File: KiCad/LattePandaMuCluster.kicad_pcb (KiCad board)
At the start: 2 copper layers, 203.2 x 170.2 mm, 721 parts, among them J1 ATX-24, J10 Bus_M.2_Socket_M, J11 Bus_M.2_Socket_M, J12 Bus_M.2_Socket_M, J13 Bus_M.2_Socket_M, J14 Bus_M.2_Socket_M, J15 Conn_02x05_Odd_Even, J17 Conn_01x04, J18 Conn_01x04, J19 RJ45_LED_Shielded_x2, J2 Conn_02x04_Top_Bottom, J20 RJE361882415, J21 RJ45_LED_Shielded_x2, J22 USB3_A_Stacked, J23 USB3_IDC, J24 Conn_02x05_Odd_Even, J26 HDMI_A, J27 JACK-USBE-20PINTL, J3 SFF-8087, J4 SFF-8087, J5 SATA, J6 Bus_M.2_Socket_E, J7 Bus_M.2_Socket_E, J8 Bus_PCI_Express_x4, J9 Bus_PCI_Express_x4, M1 Fan_4pin, M10 Fan_4pin, M2 Fan_4pin, M3 Fan_4pin, M4 Fan_4pin, M5 Fan_4pin, M6 Fan_4pin, M7 Fan_4pin, M8 Fan_4pin, M9 Fan_4pin, Q1 2N7002, Q2 2N7002, Q3 2N7002, U1 ZD25Q64BSIGT, U10 H5VU25U, U11 H5VU25U, U12 KTI226V, U13 KTI226V, U14 ZD25Q64BSIGT, U15 ZD25Q64BSIGT, U16 H5VU25U, U17 H5VU25U, U18 H5VU25U, U19 H5VU25U, U2 ZD25Q64BSIGT, U20 KTI226V, U21 KTI226V, U22 ZD25Q64BSIGT, U23 ZD25Q64BSIGT, U24 H5VU25U, U25 H5VU25U, U26 KTI226V, U27 ZD25Q64BSIGT, U28 H5VU25U, U29 H5VU25U, U3 ZD25Q64BSIGT, U30 H5VU25U, U31 H5VU25U, U32 H5VU25U, U33 H5VU25U, U34 H5VU25U, U35 H5VU25U, U36 H5VU25U, U37 H5VU25U, U38 H5VU25U, U39 H5VU25U, U4 ZD25Q64BSIGT, U40 TPS65987DDJRSHR, U41 H5VU25U, U42 H5VU25U, U43 ZD25Q64BSIGT, U44 H5VU25U, U5 ZD25Q64BSIGT, U6 TPS54331, U7 STM32F030C8Tx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

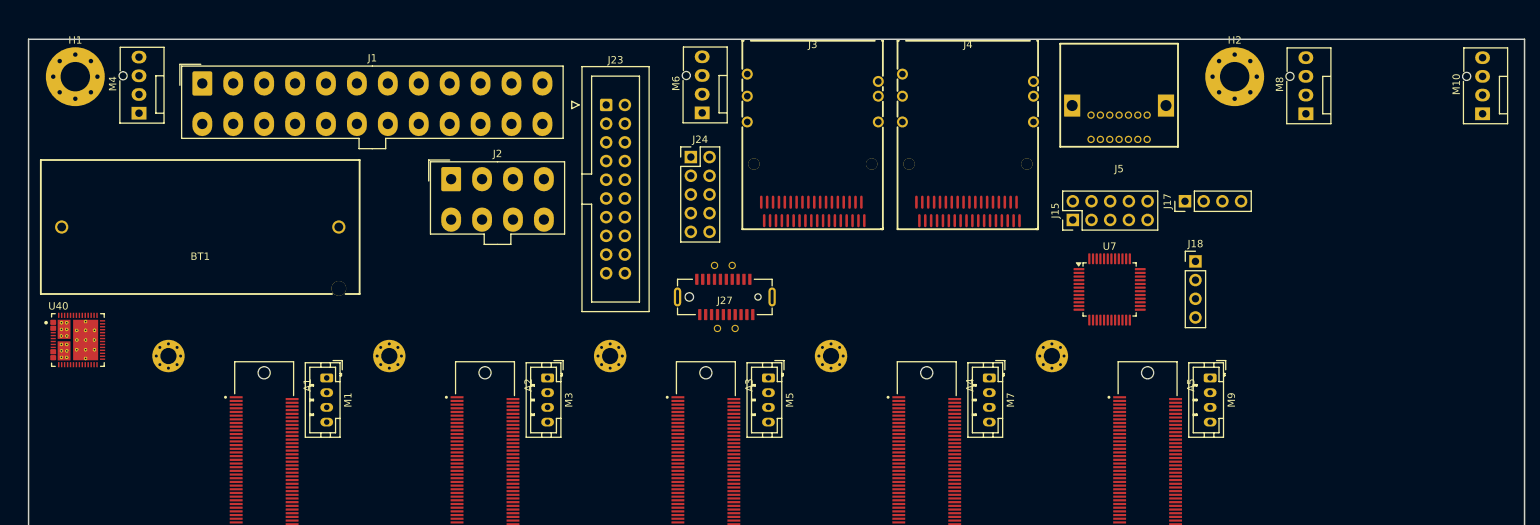
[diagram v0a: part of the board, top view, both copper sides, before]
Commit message: Lay out Headers
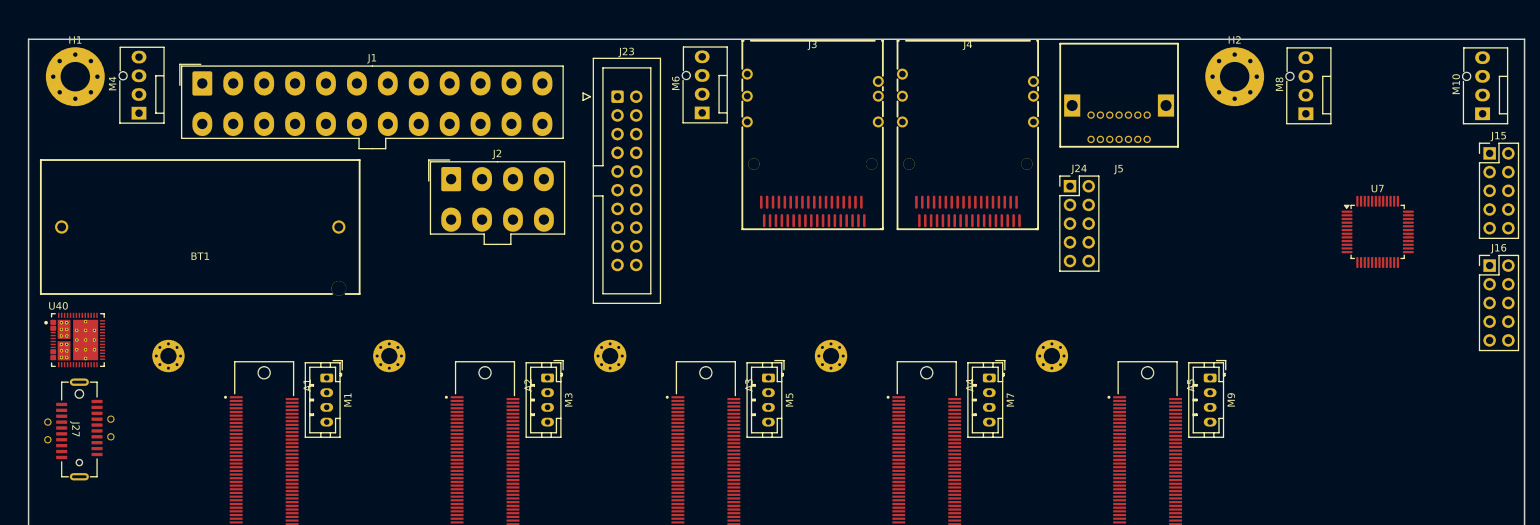
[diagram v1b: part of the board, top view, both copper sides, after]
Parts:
- removed J17, J18: Conn_01x04, Connector_PinHeader_2.54mm:PinHeader_1x04_P2.54mm_Vertical
- added J16: Conn_02x05_Odd_Even, Connector_PinHeader_2.54mm:PinHeader_2x05_P2.54mm_Vertical, F.Cu at (298.5, 80.7)
- moved J27 89.5 mm to (106.9, 103.0), turned to 90 degrees
- moved J15 57.3 mm to (298.5, 65.5), turned to 0 degrees
- moved J24 51.7 mm to (241.5, 70.0)
- moved U7 37.2 mm to (283.2, 76.2)
- moved J23 1.90 mm to (180.0, 57.8)
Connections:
- net /Module 1/TYPE_C_HEADER.SBU1 renamed /Module 1/TYPE_C_HEADER.SBU2
- J15 pad 9: unconnected-(J15-Pin_9-Pad9) -> +5VSB

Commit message: Start placing capacitors
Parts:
- moved C4 217.7 mm to (126.0, 102.5)
- moved C3 217.6 mm to (126.0, 101.5)
- moved D27 206.3 mm to (283.5, 67.0)
- moved L1 171.5 mm to (155.5, 79.5), turned to 180 degrees
- moved U6 166.7 mm to (154.0, 70.0), turned to -90 degrees
- moved U43 88.2 mm to (114.0, 106.5), turned to -90 degrees
- moved J1 47.9 mm to (171.2, 61.5), turned to 180 degrees
- moved U40 16.1 mm to (105.4, 106.9)
- moved J2 15.9 mm to (165.0, 83.0), turned to 90 degrees
- moved J27 10.3 mm to (105.5, 92.8)
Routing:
- net Net-(A1-HSIO0_TX-): track 0.00 -> 1.88 mm
- net Net-(A1-HSIO0_TX+): track 0.00 -> 1.75 mm
- added copper zone on In1.Cu, net GND
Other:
- copper layers 2 -> 4

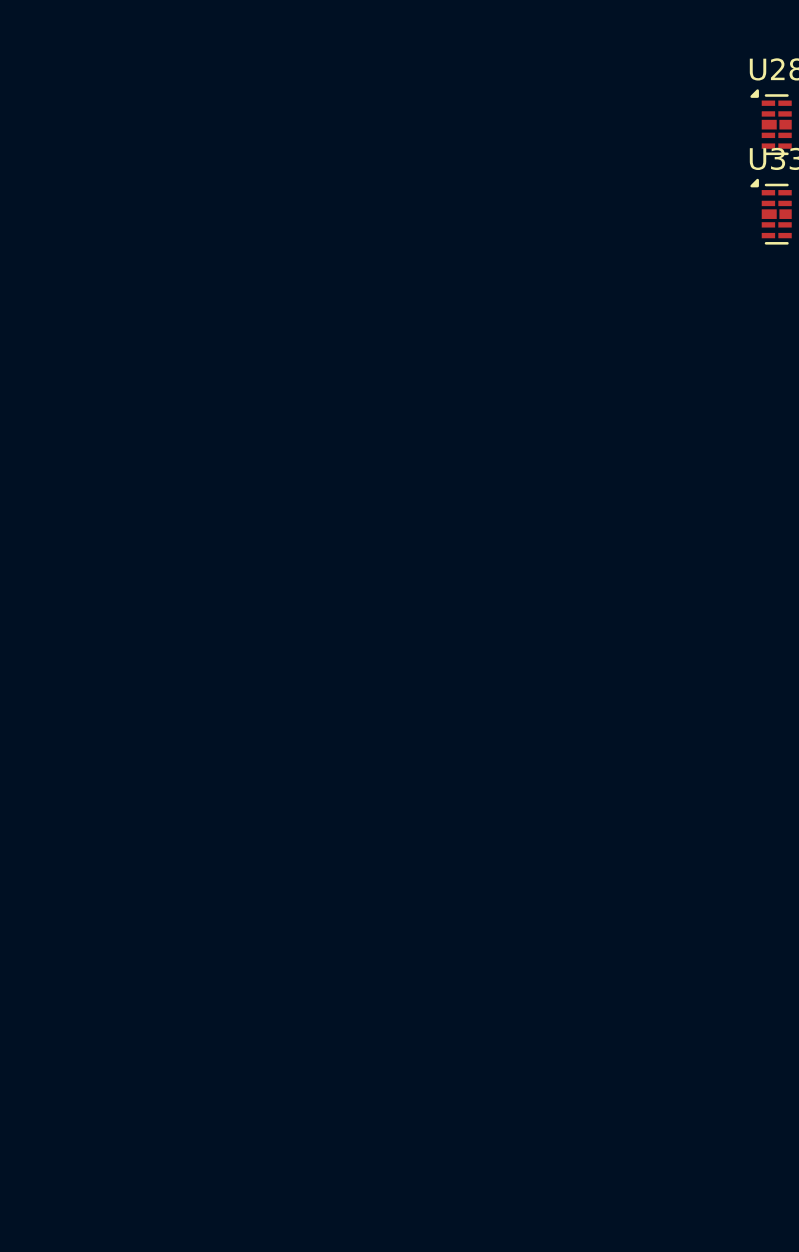
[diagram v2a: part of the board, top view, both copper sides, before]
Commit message: Finish connecting x1 slot. Add pcie clkreq lines
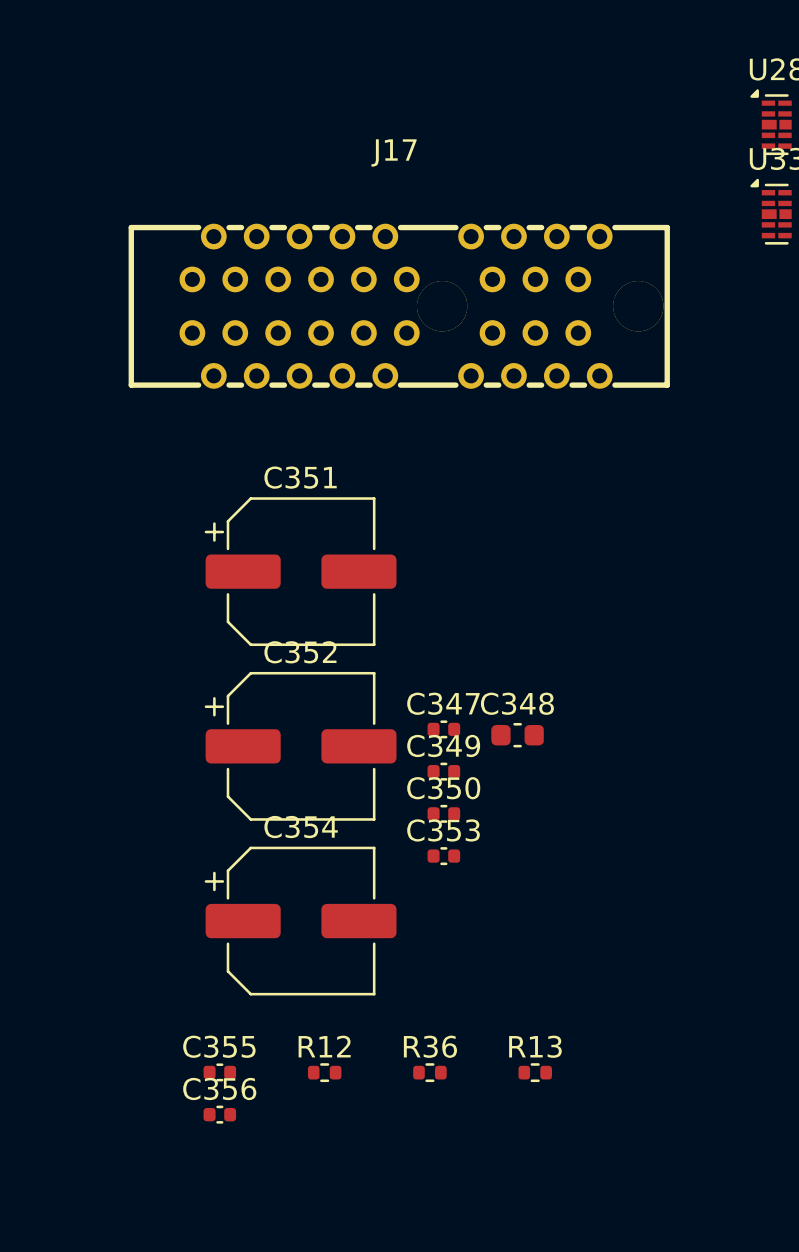
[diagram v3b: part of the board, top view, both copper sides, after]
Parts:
- added C347: 100nF/50V, Capacitor_SMD:C_0402_1005Metric, F.Cu at (60.2, 124.0)
- added C348: 10uF/10V, Capacitor_SMD:C_0603_1608Metric, F.Cu at (63.7, 124.3)
- added C349: 100nF/50V, Capacitor_SMD:C_0402_1005Metric, F.Cu at (60.2, 126.0)
- added C350: 100nF/50V, Capacitor_SMD:C_0402_1005Metric, F.Cu at (60.2, 127.9)
- added C351: 100uF/25V, Capacitor_SMD:CP_Elec_6.3x7.7, F.Cu at (53.6, 116.6)
- added C352: 100uF/25V, Capacitor_SMD:CP_Elec_6.3x7.7, F.Cu at (53.6, 124.8)
- added C353: 100nF/50V, Capacitor_SMD:C_0402_1005Metric, F.Cu at (60.2, 129.9)
- added C354: 560uF/25V, Capacitor_SMD:CP_Elec_6.3x7.7, F.Cu at (53.6, 132.9)
- added C355: 220nF, Capacitor_SMD:C_0402_1005Metric, F.Cu at (49.8, 140.0)
- added C356: 220nF, Capacitor_SMD:C_0402_1005Metric, F.Cu at (49.8, 142.0)
- added J17: Bus_PCI_Express_x1, EasyEDA2KiCAD:CONN-TH_HYCW05-PCI36-155B, F.Cu at (58.0, 104.2)
- added R12: 10k, Resistor_SMD:R_0402_1005Metric, F.Cu at (54.7, 140.0)
- added R13: 10k, Resistor_SMD:R_0402_1005Metric, F.Cu at (64.5, 140.0)
- added R36: 10k, Resistor_SMD:R_0402_1005Metric, F.Cu at (59.6, 140.0)
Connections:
- net /Module 1/TYPE_C_HEADER.SBU2 renamed /Module 1/TYPE_C_HEADER.SBU1
- net /Module 4/ETH.SMBCLK renamed /Module 4/PCIE_X4.SMBCLK
- net /Module 4/ETH.SMBDAT renamed /Module 4/PCIE_X4.SMBDAT
- A1 pad 100: Net-(A1-~{CLKREQ3}) -> /Module 1/ETH.~{CLKREQ}
- A1 pad 102: Net-(A1-~{CLKREQ4}) -> /Module 1/M2_EKEY.~{CLKREQ}
- A1 pad 25: unconnected-(A1-HSIO2_TX+-Pad25) -> Net-(A1-HSIO2_TX+)
- A1 pad 27: unconnected-(A1-HSIO2_TX--Pad27) -> Net-(A1-HSIO2_TX-)
- A1 pad 28: unconnected-(A1-HSIO2_RX+-Pad28) -> /Module 1/M2_EKEY.Rx0+
- A1 pad 30: unconnected-(A1-HSIO2_RX--Pad30) -> /Module 1/M2_EKEY.Rx0-
- A1 pad 85: /Module 1/ETH.REFCLK+ -> unconnected-(A1-REFCLK0+-Pad85)
- A1 pad 87: /Module 1/ETH.REFCLK- -> unconnected-(A1-REFCLK0--Pad87)
- A1 pad 88: unconnected-(A1-REFCLK3+-Pad88) -> /Module 1/ETH.REFCLK+
- A1 pad 90: unconnected-(A1-REFCLK3--Pad90) -> /Module 1/ETH.REFCLK-
- A1 pad 91: /Module 1/NVME.REFCLK+ -> unconnected-(A1-REFCLK1+-Pad91)
- A1 pad 93: /Module 1/NVME.REFCLK- -> unconnected-(A1-REFCLK1--Pad93)
- A1 pad 94: unconnected-(A1-REFCLK4+-Pad94) -> /Module 1/M2_EKEY.REFCLK+
- A1 pad 96: unconnected-(A1-REFCLK4--Pad96) -> /Module 1/M2_EKEY.REFCLK-
- A1 pad 97: unconnected-(A1-REFCLK2+-Pad97) -> /Module 1/NVME.REFCLK+
- A1 pad 99: unconnected-(A1-REFCLK2--Pad99) -> /Module 1/NVME.REFCLK-
- A2 pad 100: Net-(A2-~{CLKREQ3}) -> /Module 2/ETH.~{CLKREQ}
- A2 pad 102: Net-(A2-~{CLKREQ4}) -> /Module 2/M2_EKEY.~{CLKREQ}
- A2 pad 85: /Module 2/ETH.REFCLK+ -> unconnected-(A2-REFCLK0+-Pad85)
- A2 pad 87: /Module 2/ETH.REFCLK- -> unconnected-(A2-REFCLK0--Pad87)
- A2 pad 88: unconnected-(A2-REFCLK3+-Pad88) -> /Module 2/ETH.REFCLK+
- A2 pad 90: unconnected-(A2-REFCLK3--Pad90) -> /Module 2/ETH.REFCLK-
- A2 pad 91: /Module 2/NVME.REFCLK+ -> unconnected-(A2-REFCLK1+-Pad91)
- A2 pad 93: /Module 2/NVME.REFCLK- -> unconnected-(A2-REFCLK1--Pad93)
- A2 pad 94: unconnected-(A2-REFCLK4+-Pad94) -> /Module 2/M2_EKEY.REFCLK+
- A2 pad 96: unconnected-(A2-REFCLK4--Pad96) -> /Module 2/M2_EKEY.REFCLK-
- A2 pad 97: /Module 2/M2_EKEY.REFCLK+ -> /Module 2/NVME.REFCLK+
- A2 pad 99: /Module 2/M2_EKEY.REFCLK- -> /Module 2/NVME.REFCLK-
- A3 pad 100: Net-(A3-~{CLKREQ3}) -> /Module 3/ETH.~{CLKREQ}
- A3 pad 28: /Module 3/M2_EKEY.Rx0+ -> /Module 3/PCIE_X1.Rx0+
- A3 pad 30: /Module 3/M2_EKEY.Rx0- -> /Module 3/PCIE_X1.Rx0-
- A3 pad 79: /Module 3/M2_EKEY.USB-D- -> /Module 3/PCIE_X1.USB-D-
- A3 pad 81: /Module 3/M2_EKEY.USB-D+ -> /Module 3/PCIE_X1.USB-D+
- A3 pad 85: /Module 3/ETH.REFCLK+ -> unconnected-(A3-REFCLK0+-Pad85)
- A3 pad 87: /Module 3/ETH.REFCLK- -> unconnected-(A3-REFCLK0--Pad87)
- A3 pad 88: unconnected-(A3-REFCLK3+-Pad88) -> /Module 3/ETH.REFCLK+
- A3 pad 90: unconnected-(A3-REFCLK3--Pad90) -> /Module 3/ETH.REFCLK-
- A3 pad 91: /Module 3/NVME.REFCLK+ -> unconnected-(A3-REFCLK1+-Pad91)
- A3 pad 93: /Module 3/NVME.REFCLK- -> unconnected-(A3-REFCLK1--Pad93)
- A3 pad 94: unconnected-(A3-REFCLK4+-Pad94) -> /Module 3/PCIE_X1.REFCLK+
- A3 pad 96: unconnected-(A3-REFCLK4--Pad96) -> /Module 3/PCIE_X1.REFCLK-
- A3 pad 97: /Module 3/M2_EKEY.REFCLK+ -> /Module 3/NVME.REFCLK+
- A3 pad 99: /Module 3/M2_EKEY.REFCLK- -> /Module 3/NVME.REFCLK-
- A4 pad 100: Net-(A4-~{CLKREQ3}) -> /Module 4/ETH.~{CLKREQ}
- A4 pad 22: /Module 4/PCIE_X4.Rx1+ -> /Module 4/PCIE_X4.RX4+
- A4 pad 24: /Module 4/PCIE_X4.Rx1- -> /Module 4/PCIE_X4.RX4-
- A4 pad 46: /Module 4/NVME.Rx1+ -> /Module 4/NVME.RX4+
- A4 pad 48: /Module 4/NVME.Rx1- -> /Module 4/NVME.RX4-
- A4 pad 85: /Module 4/ETH.REFCLK+ -> unconnected-(A4-REFCLK0+-Pad85)
- A4 pad 87: /Module 4/ETH.REFCLK- -> unconnected-(A4-REFCLK0--Pad87)
- A4 pad 88: unconnected-(A4-REFCLK3+-Pad88) -> /Module 4/ETH.REFCLK+
- A4 pad 90: unconnected-(A4-REFCLK3--Pad90) -> /Module 4/ETH.REFCLK-
- A4 pad 91: /Module 4/NVME.REFCLK+ -> unconnected-(A4-REFCLK1+-Pad91)
- A4 pad 93: /Module 4/NVME.REFCLK- -> unconnected-(A4-REFCLK1--Pad93)
- A4 pad 94: unconnected-(A4-REFCLK4+-Pad94) -> /Module 4/PCIE_X4.REFCLK+
- A4 pad 96: unconnected-(A4-REFCLK4--Pad96) -> /Module 4/PCIE_X4.REFCLK-
- A4 pad 97: /Module 4/PCIE_X4.REFCLK+ -> /Module 4/NVME.REFCLK+
- A4 pad 99: /Module 4/PCIE_X4.REFCLK- -> /Module 4/NVME.REFCLK-
- A5 pad 100: Net-(A5-~{CLKREQ3}) -> /Module 5/ETH.~{CLKREQ}
- A5 pad 85: /Module 5/ETH.REFCLK+ -> unconnected-(A5-REFCLK0+-Pad85)
- A5 pad 87: /Module 5/ETH.REFCLK- -> unconnected-(A5-REFCLK0--Pad87)
- A5 pad 88: unconnected-(A5-REFCLK3+-Pad88) -> /Module 5/ETH.REFCLK+
- A5 pad 90: unconnected-(A5-REFCLK3--Pad90) -> /Module 5/ETH.REFCLK-
- A5 pad 91: /Module 5/NVME.REFCLK+ -> unconnected-(A5-REFCLK1+-Pad91)
- A5 pad 93: /Module 5/NVME.REFCLK- -> unconnected-(A5-REFCLK1--Pad93)
- A5 pad 94: unconnected-(A5-REFCLK4+-Pad94) -> /Module 5/PCIE_X4.REFCLK+
- A5 pad 96: unconnected-(A5-REFCLK4--Pad96) -> /Module 5/PCIE_X4.REFCLK-
- A5 pad 97: /Module 5/PCIE_X4.REFCLK+ -> /Module 5/NVME.REFCLK+
- A5 pad 99: /Module 5/PCIE_X4.REFCLK- -> /Module 5/NVME.REFCLK-
- C63 pad 1: /Module 3/M2_EKEY.Tx0+ -> /Module 3/PCIE_X1.Tx0+
- C64 pad 1: /Module 3/M2_EKEY.Tx0- -> /Module 3/PCIE_X1.Tx0-
- C84 pad 1: /Module 4/PCIE_X4.Tx1+ -> /Module 4/PCIE_X4.TX4+
- C85 pad 1: /Module 4/PCIE_X4.Tx1- -> /Module 4/PCIE_X4.TX4-
- C92 pad 1: /Module 4/NVME.Tx1+ -> /Module 4/NVME.TX4+
- C93 pad 1: /Module 4/NVME.Tx1- -> /Module 4/NVME.TX4-
- J7 pad 3: /Module 3/M2_EKEY.USB-D+ -> /Module 1/M2_EKEY.USB-D+
- J7 pad 35: /Module 3/M2_EKEY.Tx0+ -> /Module 1/M2_EKEY.Tx0+
- J7 pad 37: /Module 3/M2_EKEY.Tx0- -> /Module 1/M2_EKEY.Tx0-
- J7 pad 41: /Module 3/M2_EKEY.Rx0+ -> /Module 1/M2_EKEY.Rx0+
- J7 pad 43: /Module 3/M2_EKEY.Rx0- -> /Module 1/M2_EKEY.Rx0-
- J7 pad 47: /Module 3/M2_EKEY.REFCLK+ -> /Module 1/M2_EKEY.REFCLK+
- J7 pad 49: /Module 3/M2_EKEY.REFCLK- -> /Module 1/M2_EKEY.REFCLK-
- J7 pad 5: /Module 3/M2_EKEY.USB-D- -> /Module 1/M2_EKEY.USB-D-
- J7 pad 50: /Module 3/NVME.SUSCLK -> /Module 1/M2_EKEY.SUSCLK
- J7 pad 52: /Module 3/NVME.~{PLTRST} -> /Module 1/NVME.~{PLTRST}
- J7 pad 55: /Module 3/NVME.~{WAKE} -> /Module 1/NVME.~{WAKE}
